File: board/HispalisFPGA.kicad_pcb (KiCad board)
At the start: 4 copper layers, 90 x 102.1 mm, 135 parts, among them J1 HC-TYPE-C-16P-01A, Q1 DMG1012T, Q2 DMG1012T, Q3 DMG1012T, Q4 DMG1012T, SW1 SW_DIP_x08, U1 93LC46B, U2 FT2232HQ, Y1 12MHz

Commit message: Complete schematic
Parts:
- removed C47, C49, C51, C52: 100nF, Capacitor_SMD:C_0402_1005Metric
- removed C48, C50: 10nF, Capacitor_SMD:C_0402_1005Metric
- C11, C21, C23, C46: value 10nF -> 100nF
- C12, C15, C40, C42: value 100nF -> 10nF
- C14: value 10nF -> 22uF; footprint Capacitor_SMD:C_0402_1005Metric -> Capacitor_SMD:C_0603_1608Metric
- C16: value 10nF -> 1uF
- C18: value 100nF -> 1nF
- C19: value 1uF -> 1nF
- C20: value 22uF -> 1uF; footprint Capacitor_SMD:C_0603_1608Metric -> Capacitor_SMD:C_0402_1005Metric
- C24: value 1uF -> 100nF
- C25: value 1nF -> 4.7uF
- C26: value 1nF -> 100nF
- C27: value 100nF -> 4.7uF
- C28, C29: value 100nF -> 10pF
- C31, C33: value 4.7uF -> 100nF
- C32: value 100nF -> 3.3uF
- C34, C35: value 10pF -> 100nF
- C38: value 3.3uF -> 10nF
- FPGA1: value LFE5UM-381 -> LFE5U-25F
- moved R14 56.3 mm to (92.5, 71.5), turned to 0 degrees
- moved C22 36.2 mm to (54.1, 60.5)
- moved C23 36.2 mm to (54.1, 62.5)
- moved C25 35.0 mm to (54.1, 64.4)
- moved C45 31.2 mm to (70.7, 73.5)
- moved C46 31.2 mm to (70.7, 75.5)
- moved C44 30.5 mm to (75.5, 73.5)
- moved C18 28.5 mm to (59.0, 65.5)
- moved C14 27.5 mm to (59.6, 58.8)
- moved C21 26.8 mm to (54.1, 58.5)
- moved C15 24.9 mm to (63.0, 60.5)
- moved CLK1 22.4 mm to (135.4, 119.3)
- moved C16 17.8 mm to (59.6, 61.3)
- moved C12 16.2 mm to (63.0, 58.5)
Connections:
- C10 pad 1: +1V1 -> Net-(SW_REG2-VBST)
- C10 pad 2: GND -> Net-(SW_REG2-SW)
- C13 pad 1: Net-(SW_REG2-VBST) -> +1V1
- C13 pad 2: Net-(SW_REG2-SW) -> GND
- C16 pad 1: +1V1 -> +5V
- C19 pad 1: +5V -> +1V1
- C20 pad 1: +1V1 -> +2V5
- C21 pad 1: +1V1 -> Net-(J1-SHIELD)
- C22 pad 1: +1V1 -> Net-(ESD2-VBIAS)
- C23 pad 1: +1V1 -> +3.3V
- C24 pad 1: +2V5 -> Net-(U2-VREGOUT)
- C25 pad 1: +1V1 -> Net-(U2-VPLL)
- C26 pad 1: +1V1 -> Net-(U2-VREGOUT)
- C27 pad 1: Net-(J1-SHIELD) -> Net-(U2-VPHY)
- C28 pad 1: Net-(ESD2-VBIAS) -> GND
- C28 pad 2: GND -> Net-(U2-OSCI)
- C29 pad 1: +3.3V -> GND
- C29 pad 2: GND -> Net-(U2-OSCO)
- C34 pad 1: GND -> +3.3V
- C34 pad 2: Net-(U2-OSCI) -> GND
- C35 pad 1: GND -> +3.3V
- C35 pad 2: Net-(U2-OSCO) -> GND
- C36 pad 1: Net-(U2-VREGOUT) -> +3.3V
- C37 pad 1: Net-(U2-VPLL) -> +3V3
- C38 pad 1: Net-(U2-VREGOUT) -> +3V3
- C39 pad 1: Net-(U2-VPHY) -> +3V3
- C40 pad 1: +3.3V -> +3V3
- C41 pad 1: +3.3V -> +3V3
- C42 pad 1: +3.3V -> +3V3
- FPGA1 pad T10: +1V1 -> GND
- FPGA1 pad T11: +1V1 -> GND
- FPGA1 pad T12: +1V1 -> GND
- FPGA1 pad T13: +1V1 -> GND
- FPGA1 pad T14: +1V1 -> GND
- FPGA1 pad T15: +1V1 -> GND
- FPGA1 pad T6: +1V1 -> GND
- FPGA1 pad T7: +1V1 -> GND
- FPGA1 pad T8: +1V1 -> GND
- FPGA1 pad T9: +1V1 -> GND
- FPGA1 pad U15: +1V1 -> GND
- FPGA1 pad U6: +1V1 -> GND
- FPGA1 pad V10: +2V5 -> GND
- FPGA1 pad V11: +2V5 -> GND
- FPGA1 pad V17: +2V5 -> GND
- FPGA1 pad V18: +2V5 -> GND
- FPGA1 pad W20: unconnected-(FPGA1K-REFCLKN_D1-PadW20) -> GND
- FPGA1 pad Y11: unconnected-(FPGA1J-REFCLKP_D0-PadY11) -> GND
- FPGA1 pad Y12: unconnected-(FPGA1J-REFCLKN_D0-PadY12) -> GND
- FPGA1 pad Y14: unconnected-(FPGA1K-HDRXP0_D1CH0-PadY14) -> GND
- FPGA1 pad Y15: unconnected-(FPGA1K-HDRXN0_D1CH0-PadY15) -> GND
- FPGA1 pad Y16: unconnected-(FPGA1K-HDRXP0_D1CH1-PadY16) -> GND
- FPGA1 pad Y17: unconnected-(FPGA1K-HDRXN0_D1CH1-PadY17) -> GND
- FPGA1 pad Y19: unconnected-(FPGA1K-REFCLKP_D1-PadY19) -> GND
- FPGA1 pad Y5: unconnected-(FPGA1J-HDRXP0_D0CH0-PadY5) -> GND
- FPGA1 pad Y6: unconnected-(FPGA1J-HDRXN0_D0CH0-PadY6) -> GND
- FPGA1 pad Y7: unconnected-(FPGA1J-HDRXP0_D0CH1-PadY7) -> GND
- FPGA1 pad Y8: unconnected-(FPGA1J-HDRXN0_D0CH1-PadY8) -> GND
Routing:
- net PROGRAMN: track 19.6 -> 12.1 mm
- net +3V3: track 22.9 -> 17.8 mm
- net unconnected-(FPGA1J-REFCLKN_D0-PadY12): track 4.75 -> 0.00 mm
- net (no net): track 4.70 -> 0.00 mm

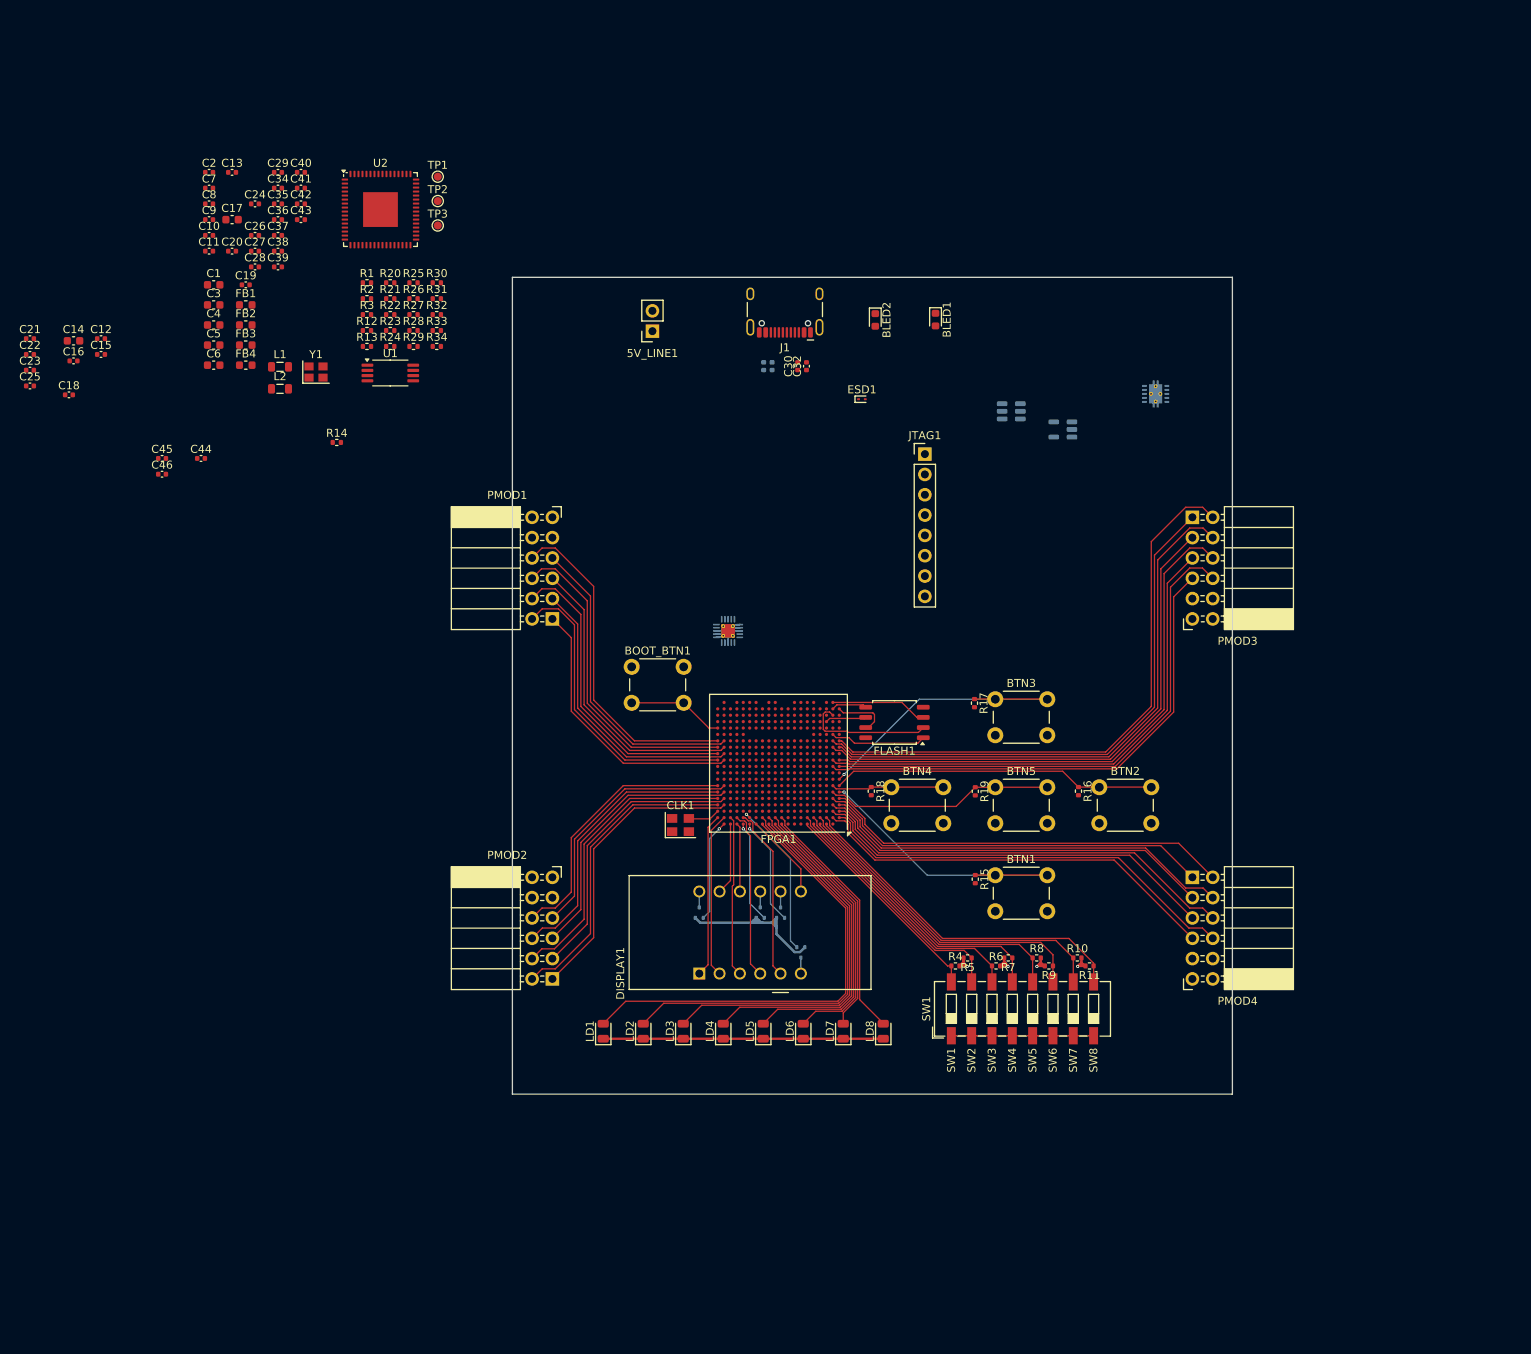
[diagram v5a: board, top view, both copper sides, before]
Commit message: Finish routing and remove unneeded silkscreen
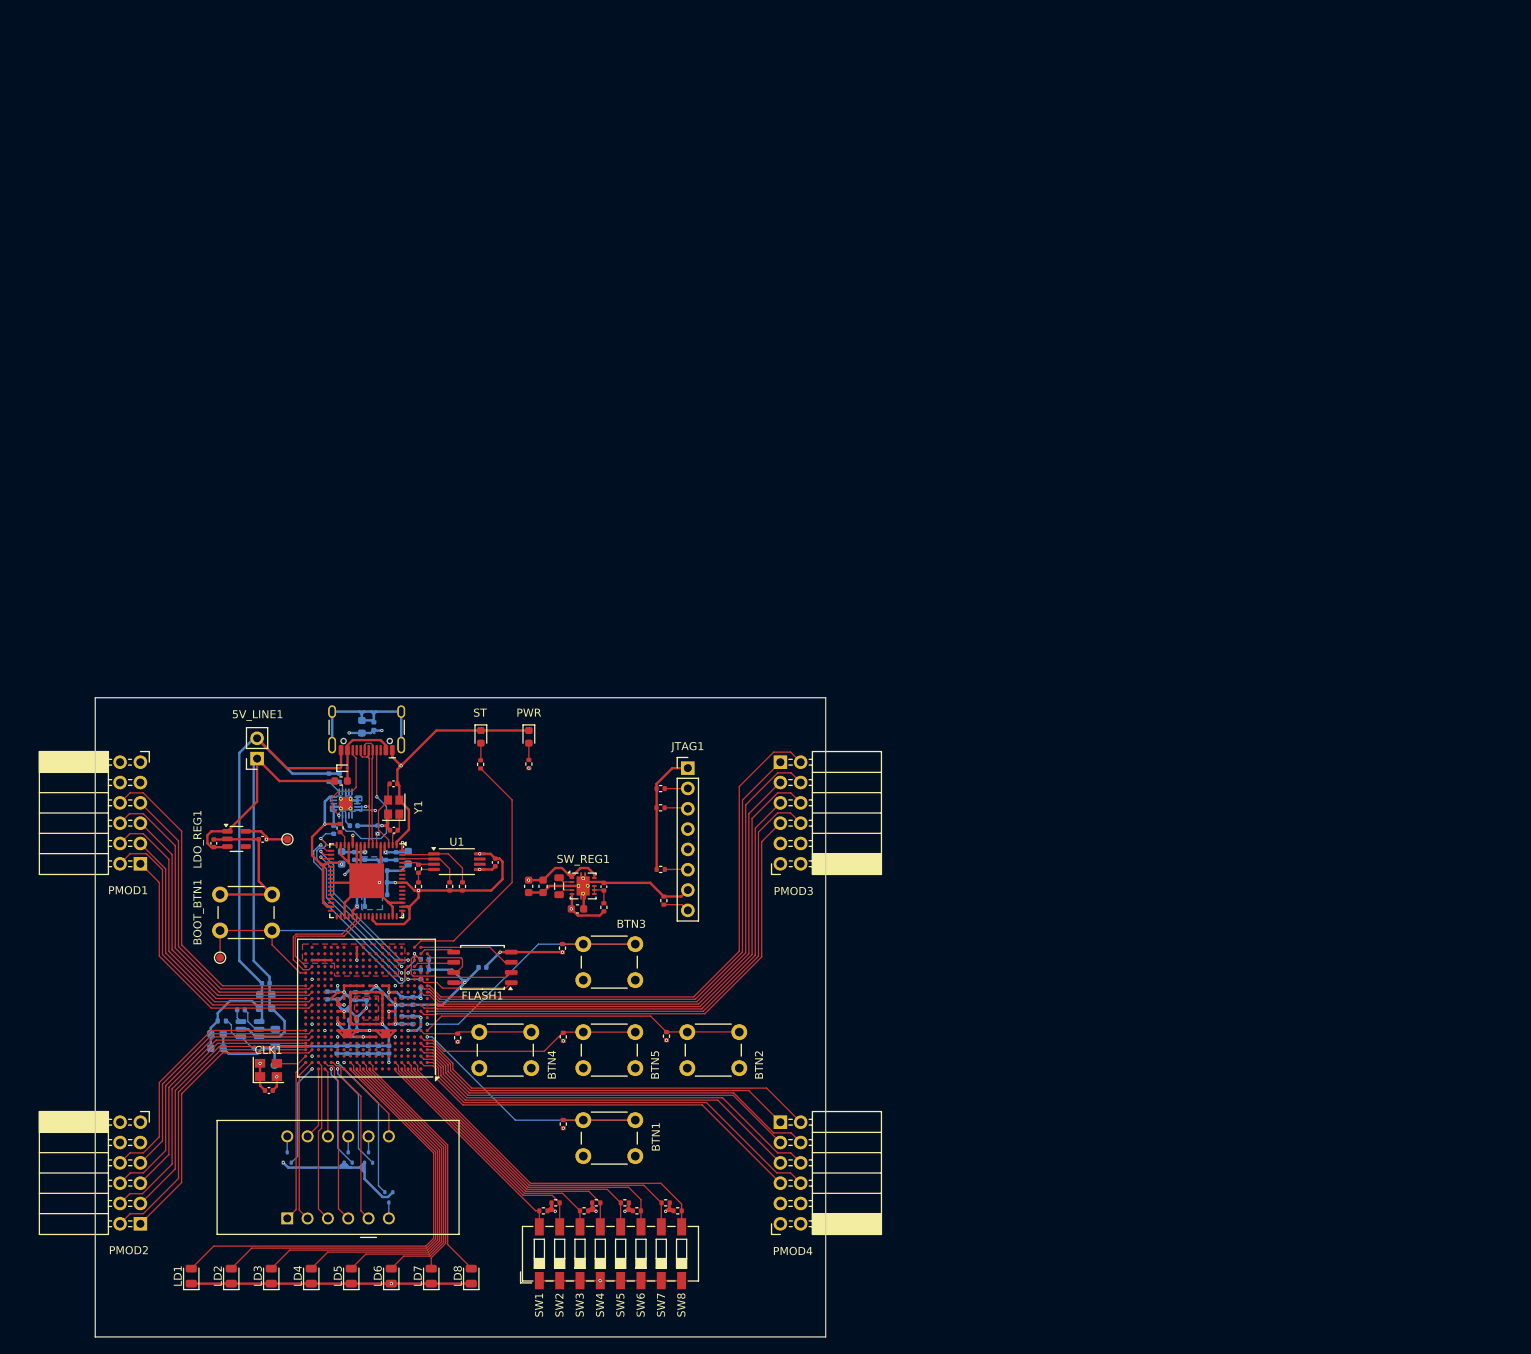
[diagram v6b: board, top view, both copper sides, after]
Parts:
- C10, C11, C12, C13, C14, C15, C17, C18, C19, C21, C22, C24, C25, C26, C27, C3, C30, C32, C34, C35, C36, C37, C38, C39, C40, C41, C42, C43, C44, C45, C5, C7, C8, C9, FB1, FB3, FB4, L2, R13, R2, R3, R31, R32, R33, R34, R8, R9, TP1: moved to B.Cu
- LDO_REG1, SW_REG1: moved to F.Cu
- moved SW_REG2 122.6 mm to (81.6, 144.8)
- moved R20 118.7 mm to (128.5, 166.6)
- moved R21 118.1 mm to (130.0, 167.6), turned to 180 degrees
- moved R22 116.2 mm to (133.6, 166.6)
- moved R23 115.8 mm to (135.1, 167.6), turned to 180 degrees
- moved LDO_REG1 115.3 mm to (80.0, 121.1), turned to 0 degrees
- moved TP1 112.9 mm to (84.7, 149.3), turned to 180 degrees
- moved C13 111.0 mm to (96.4, 147.4), turned to -90 degrees
- moved C40 106.9 mm to (102.0, 143.7), turned to 90 degrees
- moved C17 103.6 mm to (77.5, 147.2), turned to 180 degrees
- moved C11 102.3 mm to (99.0, 147.4), turned to -90 degrees
- moved C2 102.0 mm to (125.9, 127.0), turned to -90 degrees
- moved C41 101.4 mm to (96.2, 140.7), turned to -90 degrees
- moved C43 100.3 mm to (94.5, 143.7)
- moved C8 100.2 mm to (92.6, 140.6), turned to -90 degrees
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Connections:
- C23 pad 1: +3.3V -> +3V3
- C34 pad 1: +3.3V -> +3V3
- C35 pad 1: +3.3V -> +3V3
- C36 pad 1: +3.3V -> +3V3
- FB3 pad 1: +3.3V -> +3V3
- FB4 pad 1: +3.3V -> +3V3
- FPGA1 pad M3: RXD_UART -> unconnected-(FPGA1F-PL86B-PadM3)
- FPGA1 pad N3: TXD_UART -> unconnected-(FPGA1F-PL86A-PadN3)
- FPGA1 pad U19: unconnected-(FPGA1E-PR89C-PadU19) -> TXD_UART
- FPGA1 pad U20: unconnected-(FPGA1E-PR86D-PadU20) -> RXD_UART
- R10 pad 2: +3.3V -> +3V3
- R12 pad 1: +3.3V -> +3V3
- R14 pad 2: +3.3V -> +3V3
- R15 pad 1: +3.3V -> +3V3
- U1 pad 8: +3.3V -> +3V3
- U2 pad 20: +3.3V -> +3V3
- U2 pad 31: +3.3V -> +3V3
- U2 pad 42: +3.3V -> +3V3
- U2 pad 50: +3.3V -> +3V3
- U2 pad 56: +3.3V -> +3V3
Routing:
- net GND: track 81.1 -> 393.2 mm, vias 4 -> 36
- net +3V3: track 17.8 -> 158.8 mm, vias 0 -> 16
- net +5V: track 0.00 -> 123.6 mm, vias 0 -> 1
- net TDI: track 0.00 -> 85.5 mm, vias 0 -> 2
- net TDO: track 0.00 -> 77.1 mm, vias 0 -> 2
- net TCK: track 0.00 -> 71.3 mm, vias 0 -> 2
- net TMS: track 0.00 -> 67.5 mm, vias 0 -> 2
- net +2V5: track 0.00 -> 54.7 mm, vias 0 -> 5
- net +1V1: track 0.00 -> 46.6 mm, vias 0 -> 1
- net Net-(U2-VREGOUT): track 0.00 -> 36.7 mm, vias 0 -> 5
- net Net-(FPGA1I-DONE): track 0.00 -> 31.4 mm
- net PROGRAMN: track 12.1 -> 41.8 mm, vias 0 -> 1
- net Net-(J1-SHIELD): track 0.00 -> 22.1 mm
- net Net-(ESD2-C_CC1): track 0.00 -> 18.7 mm, vias 0 -> 1
- net USB_D-: track 0.00 -> 17.3 mm, vias 0 -> 1
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- added copper zone on In2.Cu, net +3V3
- added copper zone on B.Cu, net GND
- added copper zone on F.Cu, net GND
- added copper zone on In1.Cu, net GND
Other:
- board size 90 x 102.1 mm -> 91.3 x 79.9 mm
- board text added: "PWR"
- board text added: "ST"

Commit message: No errors
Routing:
- net GND: track 393.2 -> 274.7 mm
- net Net-(J1-SHIELD): track 22.1 -> 0.00 mm
- net +3V3: track 158.8 -> 140.2 mm
- net +1V1: track 46.6 -> 28.6 mm
- net Net-(U2-VREGOUT): track 36.7 -> 30.5 mm
- net +2V5: track 54.7 -> 52.7 mm
- added copper zone on F.Cu, net +1V1
- added copper zone on B.Cu, net +2V5
- added copper zone on B.Cu, net +3V3
- added copper zone on F.Cu, net +3V3
- added copper zone on B.Cu, net Net-(J1-SHIELD)
- added copper zone on B.Cu, net Net-(U2-VREGOUT)

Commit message: No warnings
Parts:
- added MH01: MountingHole_3mm, MountingHole:MountingHole_3mm, F.Cu at (65.9, 107.0)
- added MH02: MountingHole_3mm, MountingHole:MountingHole_3mm, F.Cu at (150.0, 107.0)
- added MH03: MountingHole_3mm, MountingHole:MountingHole_3mm, F.Cu at (65.9, 179.7)
- added MH04: MountingHole_3mm, MountingHole:MountingHole_3mm, F.Cu at (150.0, 179.7)
- moved PMOD1 3.63 mm to (67.9, 115.1)
- moved PMOD3 3.58 mm to (148.0, 127.8)
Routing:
- net PMOD1_9: track 40.4 -> 38.9 mm
- net PMOD1_7: track 37.8 -> 36.3 mm
- net PMOD1_8: track 39.0 -> 37.5 mm
- net PMOD1_4: track 39.0 -> 37.5 mm
- net PMOD1_3: track 37.5 -> 36.0 mm
- net PMOD1_2: track 36.0 -> 34.5 mm
- net PMOD1_1: track 34.5 -> 33.0 mm
- net PMOD1_10: track 42.0 -> 40.5 mm
- net PMOD3_8: track 70.4 -> 68.9 mm
- net PMOD3_7: track 72.5 -> 71.1 mm
- net PMOD3_9: track 68.3 -> 66.8 mm
- net PMOD3_4: track 63.4 -> 62.0 mm
- net PMOD3_3: track 65.1 -> 63.7 mm
- net PMOD3_10: track 66.6 -> 65.1 mm
- net PMOD3_1: track 69.1 -> 67.6 mm
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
